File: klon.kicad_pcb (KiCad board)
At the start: 2 copper layers, 60 x 100 mm, 71 parts, among them U1 TL072, U2 LTC1044, U3 TL072

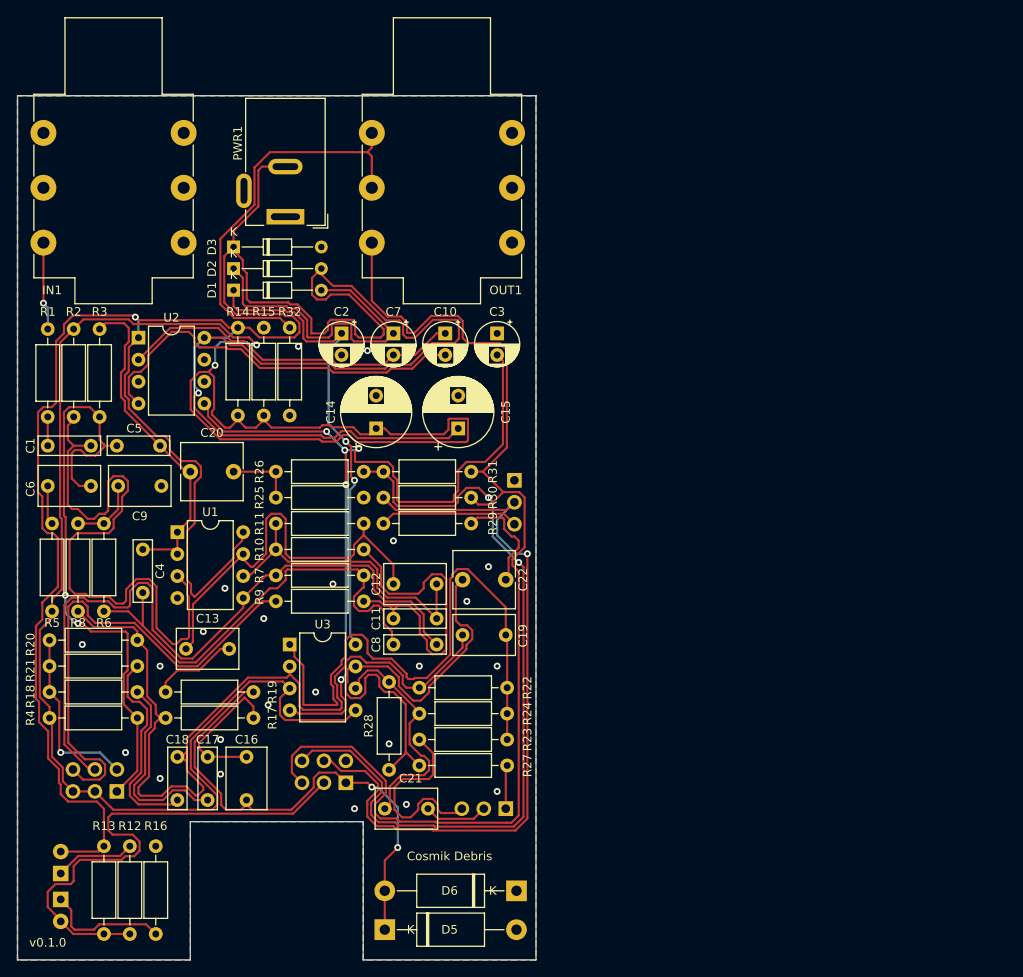
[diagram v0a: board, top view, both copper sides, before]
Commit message: update to kicad 6.0, use SMD resistors, ICs
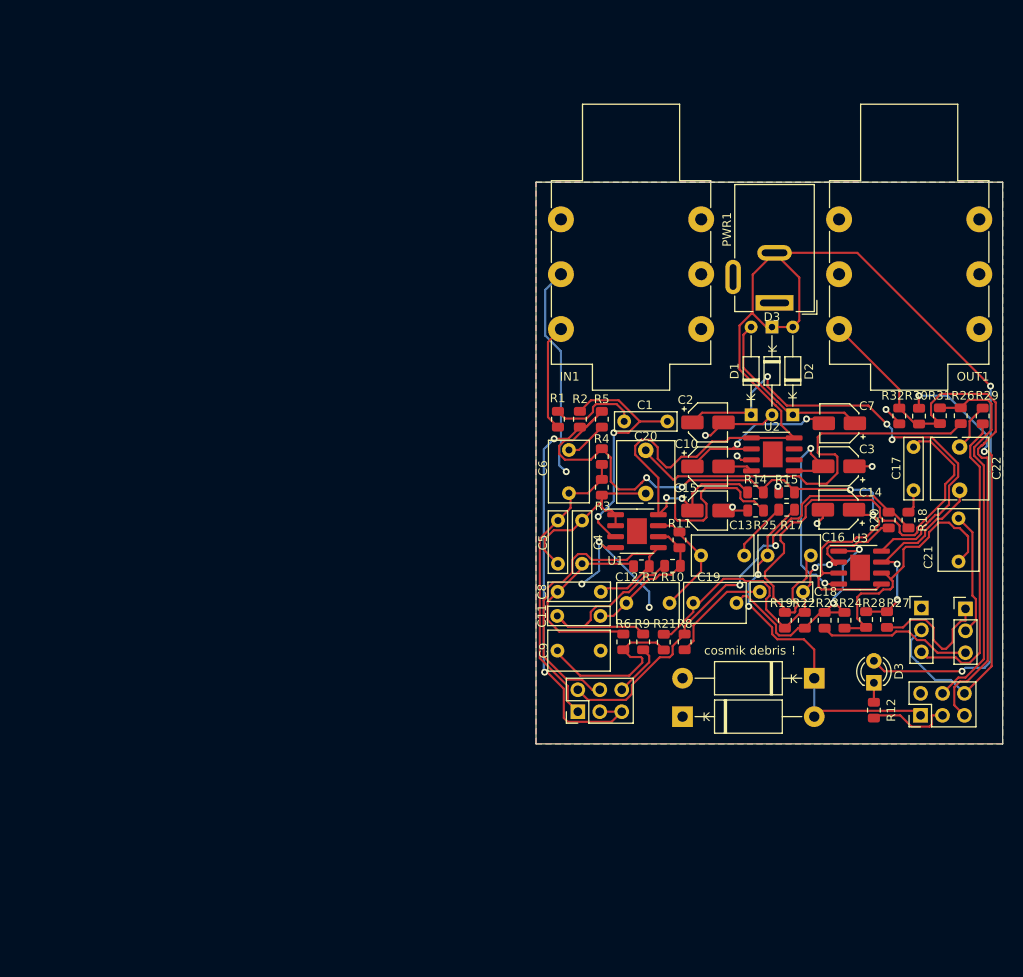
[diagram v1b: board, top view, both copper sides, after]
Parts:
- removed the D3 at (65.0, 57.5)
- removed D3_ON, D4_OFF: LED, LED_THT:LED_D3.0mm_Clear
- removed D5, D6: 1N34A, Diode_THT:D_DO-15_P15.24mm_Horizontal
- removed R13: 2K2, Resistor_THT:R_Axial_DIN0207_L6.3mm_D2.5mm_P10.16mm_Horizontal
- removed R16: 22K, Resistor_THT:R_Axial_DIN0207_L6.3mm_D2.5mm_P10.16mm_Horizontal
- added !: 1N34A, Diode_THT:D_DO-15_P15.24mm_Horizontal, F.Cu at (132.2, 107.4)
- added D3: LED, LED_THT:LED_D3.0mm_Clear, F.Cu at (139.1, 107.9)
- added D3: 1N4742, Diode_THT:D_DO-34_SOD68_P10.16mm_Horizontal, F.Cu at (127.3, 66.8)
- added cosmik debris: 1N34A, Diode_THT:D_DO-15_P15.24mm_Horizontal, F.Cu at (117.0, 111.8)
- C10, C2, C3, C7: footprint Capacitor_THT:CP_Radial_D5.0mm_P2.50mm -> Capacitor_SMD:CP_Elec_4x4.5
- C14, C15: footprint Capacitor_THT:CP_Radial_D8.0mm_P3.80mm -> Capacitor_SMD:CP_Elec_4x4.5
- GAIN, SW, TONE, VOL: moved to F.Cu
- R1, R10, R11, R14, R15, R17, R18, R19, R2, R20, R21, R22, R23, R24, R25, R26, R27, R28, R29, R3, R30, R31, R32, R4, R5, R6, R7, R8, R9: footprint Resistor_THT:R_Axial_DIN0207_L6.3mm_D2.5mm_P10.16mm_Horizontal -> Resistor_SMD:R_0805_2012Metric
- R12: value 2K2 -> 3K9; footprint Resistor_THT:R_Axial_DIN0207_L6.3mm_D2.5mm_P10.16mm_Horizontal -> Resistor_SMD:R_0805_2012Metric
- U1, U3: footprint Package_DIP:DIP-8_W7.62mm -> Package_SO:SOIC-8-1EP_3.9x4.9mm_P1.27mm_EP2.29x3mm
- U2: value LTC1044 -> LTC1044A; footprint Package_DIP:DIP-8_W7.62mm -> Package_SO:SOIC-8-1EP_3.9x4.9mm_P1.27mm_EP2.29x3mm
- moved R18 91.4 mm to (143.1, 89.1), turned to -90 degrees
- moved C17 89.2 mm to (143.7, 80.6)
- moved R20 88.1 mm to (140.8, 89.1), turned to 90 degrees
- moved R12 87.5 mm to (139.1, 111.1)
- moved C18 74.9 mm to (130.9, 97.4), turned to 180 degrees
- moved U2 74.6 mm to (127.4, 81.5)
- moved R19 72.5 mm to (128.8, 100.7), turned to 90 degrees
- moved C21 72.3 mm to (148.9, 93.9), turned to 90 degrees
- moved R32 71.3 mm to (142.0, 77.1)
- moved R29 70.5 mm to (151.7, 77.1), turned to 90 degrees
- moved R26 69.4 mm to (149.1, 77.0), turned to -90 degrees
- moved C16 69.3 mm to (131.8, 93.2), turned to 180 degrees
- moved R8 67.9 mm to (114.8, 103.2), turned to -90 degrees
- moved SW 67.0 mm to (144.5, 111.7)
- moved D2 66.9 mm to (129.7, 76.9), turned to 90 degrees
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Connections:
- OUT1 pad R: Net-(OUT1-PadR) -> GND
- OUT1 pad S: Net-(OUT1-PadR) -> GND
- R32 pad 1: Net-(OUT1-PadR) -> Net-(OUT1-PadT)
- SW pad 4: Net-(R30-Pad2) -> Net-(R26-Pad1)
- SW pad 6: Net-(R26-Pad1) -> Net-(R30-Pad2)
- U2 pad 6: Net-(U2-Pad6) -> unconnected-(U2-Pad6)
- U2 pad 7: Net-(U2-Pad7) -> unconnected-(U2-Pad7)
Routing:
- net +9V: track 329.1 -> 165.5 mm, vias 2 -> 4
- net /+4.5V: track 226.7 -> 131.2 mm, vias 2 -> 6
- net /-8.6V: track 96.1 -> 25.5 mm, vias 5 -> 2
- net GND: track 0.00 -> 64.8 mm, vias 23 -> 11
- net Net-(OUT1-PadT): track 131.4 -> 69.1 mm
- net Net-(C20-Pad2): track 7.90 -> 68.7 mm
- net Net-(C18-Pad1): track 97.6 -> 45.3 mm, vias 0 -> 2
- net Net-(GAIN1-Pad6): track 57.7 -> 6.23 mm
- net Net-(R12-Pad2): track 59.6 -> 9.76 mm
- net Net-(R26-Pad1): track 92.0 -> 43.8 mm, vias 2 -> 0
- net Net-(OUT1-PadR): track 47.5 -> 0.00 mm
- net Net-(C8-Pad1): track 84.7 -> 40.8 mm
- net Net-(C1-Pad1): track 72.6 -> 29.0 mm, vias 0 -> 2
- net Net-(C10-Pad2): track 46.0 -> 3.43 mm
- net Net-(C19-Pad1): track 69.9 -> 29.9 mm, vias 0 -> 2
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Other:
- board size 60 x 100 mm -> 54 x 65 mm
- net class Default removed
- board text removed: "Cosmik Debris"
- board text removed: "v0.1.0"
